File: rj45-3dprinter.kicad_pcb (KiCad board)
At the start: 2 copper layers, 80 x 30 mm, 15 parts, among them J1 ADXL, J2 FAN1, J3 8P8C, J4 FAN2, J5 E-MOTOR, J6 8P8C, J7 PROBE

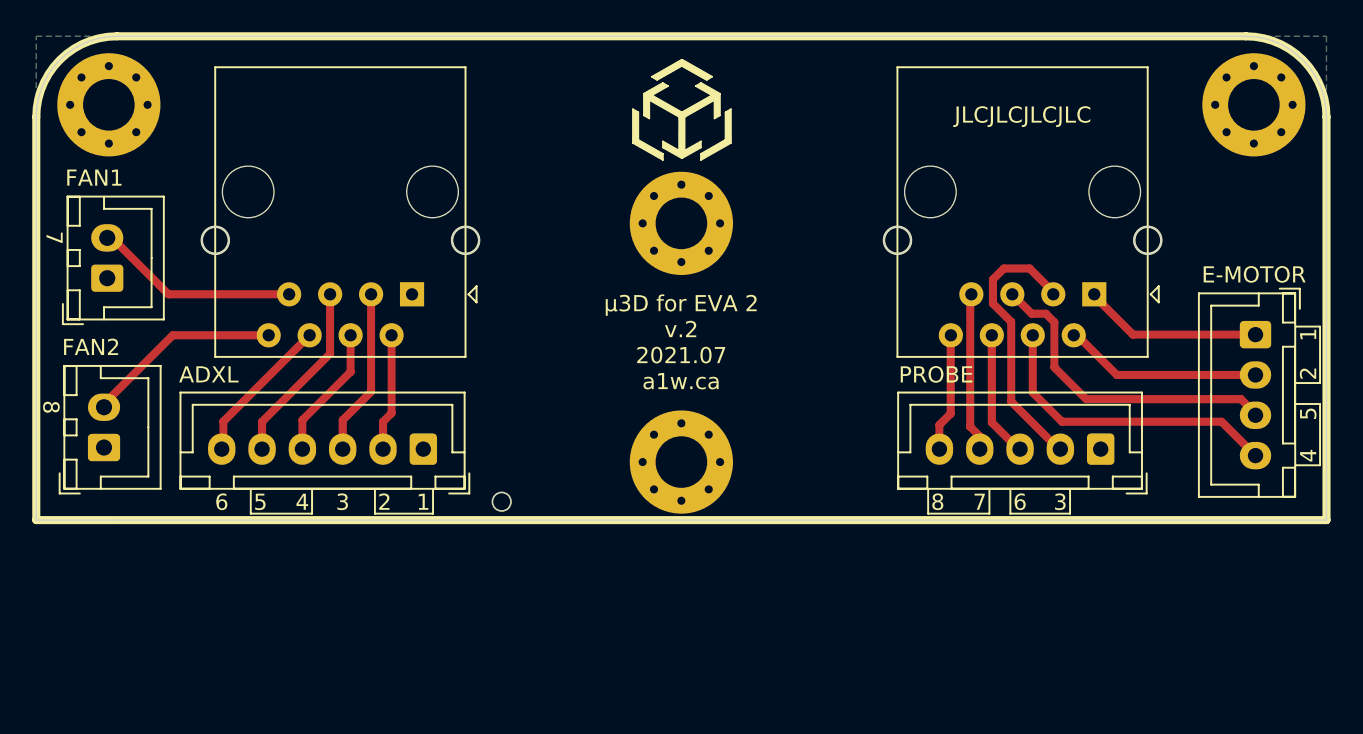
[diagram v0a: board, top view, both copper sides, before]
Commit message: Update PCB for hotend (high-current) components
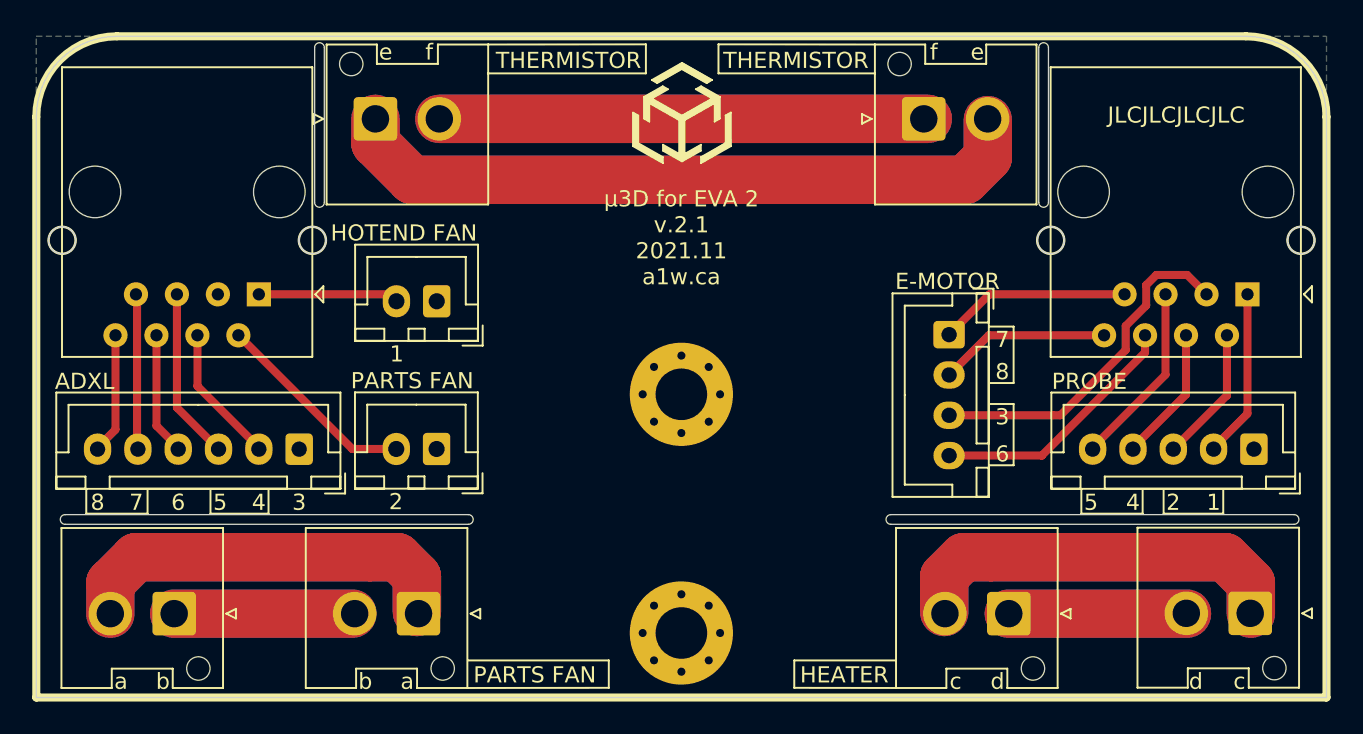
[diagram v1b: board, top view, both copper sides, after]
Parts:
- removed H3, H4: MountingHole_Pad, MountingHole:MountingHole_3.2mm_M3_Pad_Via
- added J10: THERMISTOR IN, Connector_JST:JST_VH_B2P-VH-FB-B_1x02_P3.96mm_Vertical, F.Cu at (51.0, 59.1)
- added J11: THERMISTOR OUT, Connector_JST:JST_VH_B2P-VH-FB-B_1x02_P3.96mm_Vertical, F.Cu at (85.0, 59.1)
- added J12: PARTS FAN IN, Connector_JST:JST_VH_B2P-VH-FB-B_1x02_P3.96mm_Vertical, F.Cu at (53.7, 89.8)
- added J13: PARTS FAN OUT, Connector_JST:JST_VH_B2P-VH-FB-B_1x02_P3.96mm_Vertical, F.Cu at (38.5, 89.8)
- added J8: HOTEND OUT, Connector_JST:JST_VH_B2P-VH-FB-B_1x02_P3.96mm_Vertical, F.Cu at (90.3, 89.8)
- added J9: HOTEND IN, Connector_JST:JST_VH_B2P-VH-FB-B_1x02_P3.96mm_Vertical, F.Cu at (105.3, 89.8)
- J2: value FAN1 -> HOTEND FAN
- J4: value FAN2 -> PARTS FAN
- moved J4 20.6 mm to (54.8, 79.6), turned to 180 degrees
- moved J2 20.5 mm to (54.8, 70.4), turned to 180 degrees
- moved J5 19.0 mm to (86.6, 72.5)
- moved H1 10.6 mm to (70.0, 76.2)
- moved H2 10.6 mm to (70.0, 91.0)
- moved J3 9.50 mm to (43.8, 70.0)
- moved J6 9.50 mm to (105.1, 70.0)
- moved J7 9.50 mm to (105.5, 79.6)
- moved REF** 9.50 mm to (100.5, 59.0)
- moved REF** 9.50 mm to (39.3, 57.7)
- moved J1 7.70 mm to (46.3, 79.6)
- moved G*** 0.22 mm to (70.0, 58.8)
- moved G*** 0.20 mm to (70.0, 58.8)
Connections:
- J3 pad 1: GND -> fan1-P1
- J3 pad 2: adxl-P5 -> fan2-P1
- J3 pad 3: adxl-P4 -> GND
- J3 pad 4: adxl-P3 -> adxl-P5
- J3 pad 5: adxl-P2 -> adxl-P4
- J3 pad 6: adxl-P1 -> adxl-P3
- J3 pad 7: fan1-P1 -> adxl-P2
- J3 pad 8: fan2-P1 -> adxl-P1
- J6 pad 1: extruder-P4 -> blt-P4
- J6 pad 2: extruder-P3 -> blt-P3
- J6 pad 3: blt-P4 -> extruder-P2
- J6 pad 4: extruder-P1 -> blt-P2
- J6 pad 5: extruder-P2 -> blt-P1
- J6 pad 6: blt-P3 -> extruder-P1
- J6 pad 7: blt-P2 -> extruder-P4
- J6 pad 8: blt-P1 -> extruder-P3
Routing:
- net tmp-P1: track 0.00 -> 86.6 mm
- net tmp-P2: track 0.00 -> 60.6 mm
- net hot-P1: track 0.00 -> 48.6 mm
- net fan2-P3: track 0.00 -> 48.6 mm
- net fan2-P2: track 0.00 -> 22.1 mm
- net hot-P2: track 0.00 -> 22.1 mm
- net blt-P4: track 16.9 -> 10.5 mm
- net fan1-P1: track 12.7 -> 8.81 mm
- net blt-P1: track 7.59 -> 11.4 mm
- net extruder-P1: track 19.0 -> 16.0 mm
- net adxl-P1: track 9.68 -> 7.42 mm
- net extruder-P3: track 12.7 -> 10.6 mm
- net adxl-P2: track 11.6 -> 9.67 mm
- net extruder-P2: track 19.9 -> 21.8 mm
- net blt-P2: track 10.3 -> 8.46 mm
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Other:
- board size 80 x 30 mm -> 80 x 41 mm
- board text added: "HEATER"
- board text added: "PARTS FAN"
- board text added: "THERMISTOR"
- board text added: "a"
- board text added: "b"
- board text added: "c"
- board text added: "d"
- board text added: "e"
- board text added: "f"
- board text added: "μ3D for EVA 2 v.2.1 2021.11 a1w.ca"
- board text removed: "μ3D for EVA 2 v.2 2021.07 a1w.ca"
